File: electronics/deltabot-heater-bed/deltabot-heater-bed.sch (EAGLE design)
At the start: 61 parts

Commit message: updated HBP files
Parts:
- removed SJ1, SJ2: SOLDERJUMPERNC, SparkFun-Passives:SOLDERJUMPERNC
- added R12, R20: 0, Hoektronics:RESISTOR0805
- R10, R11, R13, R14, R15, R16, R17, R18, R19, R21, R22, R23, R24, R25, R26, R27, R5, R6, R7, R8, R9: value (none) -> 1K
- R2: value (none) -> 1206 Thermistor 100K
- R3: value (none) -> 0805 Thermistor 100K
- R4: value (none) -> 0603 Thermistor 100K
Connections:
- net 12V: now also R12.1; no longer SJ1.2
- net HEATER: now also R12.2, R20.2; no longer SJ1.1, SJ2.1
- net PGND: now also R20.1; no longer SJ2.2
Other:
- moved on the sheet: R2, R3, R4, TEMP

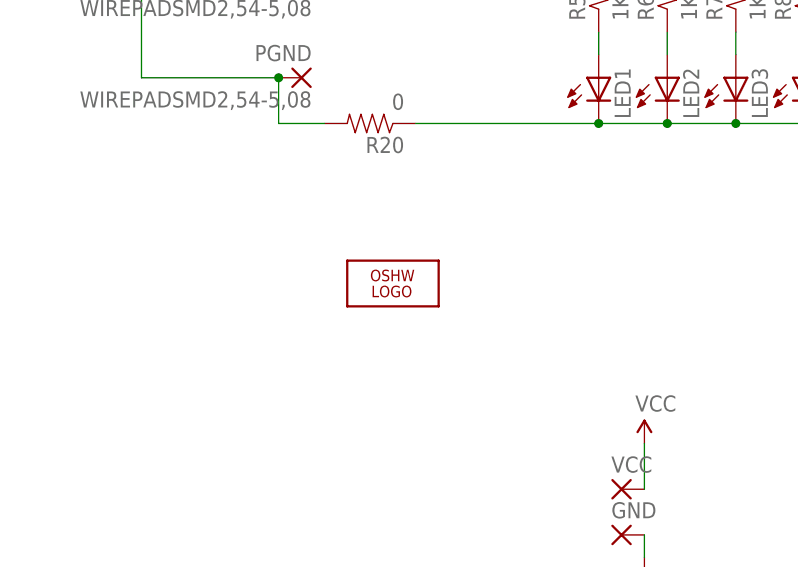
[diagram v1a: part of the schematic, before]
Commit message: Fixed HBP outline width for gerber export
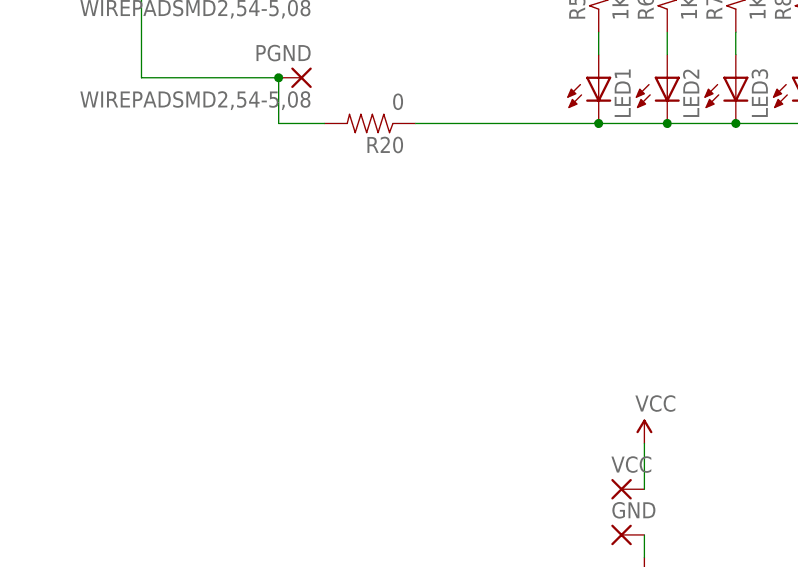
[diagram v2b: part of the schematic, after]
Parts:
- removed LOGO1: OSHW_LOGO_FILLX1000-NT, ohw-logo:OSHW_LOGO_FILLX1000-NT
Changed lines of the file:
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@@
 <?xml version="1.0" encoding="utf-8"?>
 <!DOCTYPE eagle SYSTEM "eagle.dtd">
-<eagle version="6.4">
+<eagle version="6.3">
 <drawing>
 <settings>
@@
 <part name="LED23" library="Hoektronics" deviceset="LED" device="0805"/>
 <part name="R27" library="Hoektronics" deviceset="RESISTOR" device="0805" value="1K"/>
-<part name="LOGO1" library="ohw-logo" deviceset="OSHW_LOGO_FILL" device="X1000-NT"/>
 <part name="FRAME1" library="frames" deviceset="A4L-LOC" device=""/>
 <part name="R12" library="Hoektronics" deviceset="RESISTOR" device="0805" value="0"/>
@@
 <instance part="LED23" gate="G$1" x="233.68" y="116.84"/>
 <instance part="R27" gate="G$1" x="233.68" y="127" rot="R90"/>
-<instance part="LOGO1" gate="G$1" x="58.42" y="93.98"/>
 <instance part="FRAME1" gate="G$1" x="0" y="0"/>
 <instance part="R12" gate="G$1" x="55.88" y="132.08" rot="R180"/>
